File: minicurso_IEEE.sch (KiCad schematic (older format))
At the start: 5 parts

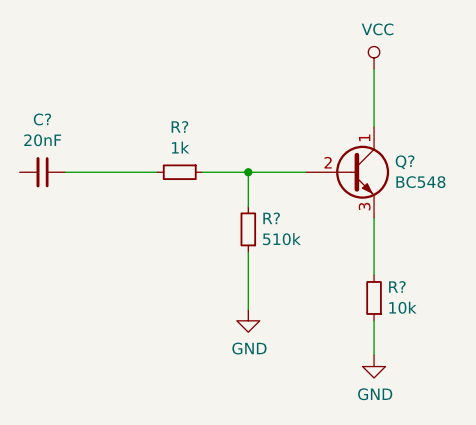
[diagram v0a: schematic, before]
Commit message: Parte-1 footprints
Foi adicionado os footprints dos componentes da primeira parte do projeto
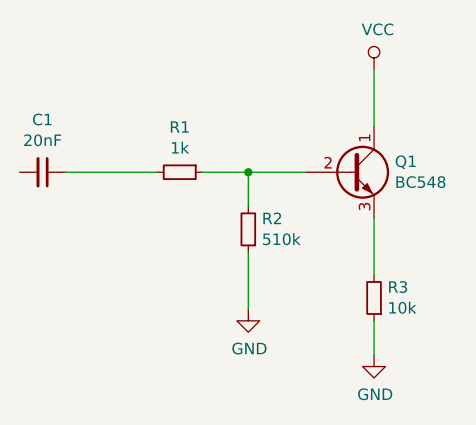
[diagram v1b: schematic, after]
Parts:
- C1: renamed from C?; footprint (none) -> Capacitor_THT:C_Disc_D3.0mm_W2.0mm_P2.50mm
- R1, R2, R3: renamed from R?; footprint (none) -> Resistor_THT:R_Axial_DIN0204_L3.6mm_D1.6mm_P7.62mm_Horizontal
- gave numbers to parts that had none: 1
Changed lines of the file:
@@
 $EndDescr
 $Comp
-L Device:R_Small R?
+L Device:R_Small R1
 U 1 1 5D4DF610
 P 1500 1700
-F 0 "R?" V 1304 1700 50  0000 C CNN
+F 0 "R1" V 1304 1700 50  0000 C CNN
 F 1 "1k" V 1395 1700 50  0000 C CNN
-F 2 "" H 1500 1700 50  0001 C CNN
+F 2 "Resistor_THT:R_Axial_DIN0204_L3.6mm_D1.6mm_P7.62mm_Horizontal" H 1500 1700 50  0001 C CNN
 F 3 "~" H 1500 1700 50  0001 C CNN
 	1    1500 1700
@@
 $EndComp
 $Comp
-L Device:C_Small C?
+L Device:C_Small C1
 U 1 1 5D4E0DE7
 P 900 1700
-F 0 "C?" V 671 1700 50  0000 C CNN
+F 0 "C1" V 671 1700 50  0000 C CNN
 F 1 "20nF" V 762 1700 50  0000 C CNN
-F 2 "" H 900 1700 50  0001 C CNN
+F 2 "Capacitor_THT:C_Disc_D3.0mm_W2.0mm_P2.50mm" H 900 1700 50  0001 C CNN
 F 3 "~" H 900 1700 50  0001 C CNN
 	1    900  1700
@@
 $EndComp
 $Comp
-L Device:R_Small R?
+L Device:R_Small R2
 U 1 1 5D4E1584
 P 1800 1950
-F 0 "R?" H 1741 1904 50  0000 R CNN
+F 0 "R2" H 1741 1904 50  0000 R CNN
 F 1 "510k" H 1741 1995 50  0000 R CNN
-F 2 "" H 1800 1950 50  0001 C CNN
+F 2 "Resistor_THT:R_Axial_DIN0204_L3.6mm_D1.6mm_P7.62mm_Horizontal" H 1800 1950 50  0001 C CNN
 F 3 "~" H 1800 1950 50  0001 C CNN
 	1    1800 1950
@@
 $EndComp
 $Comp
-L Transistor_BJT:BC548 Q?
+L Transistor_BJT:BC548 Q1
 U 1 1 5D4E1B29
 P 2250 1700
-F 0 "Q?" H 2441 1746 50  0000 L CNN
+F 0 "Q1" H 2441 1746 50  0000 L CNN
 F 1 "BC548" H 2441 1655 50  0000 L CNN
 F 2 "Package_TO_SOT_THT:TO-92_Inline" H 2450 1625 50  0001 L CIN
@@
 $EndComp
 $Comp
-L Device:R_Small R?
+L Device:R_Small R3
 U 1 1 5D4E20CF
 P 2350 2250
-F 0 "R?" H 2291 2204 50  0000 R CNN
+F 0 "R3" H 2291 2204 50  0000 R CNN
 F 1 "10k" H 2291 2295 50  0000 R CNN
-F 2 "" H 2350 2250 50  0001 C CNN
+F 2 "Resistor_THT:R_Axial_DIN0204_L3.6mm_D1.6mm_P7.62mm_Horizontal" H 2350 2250 50  0001 C CNN
 F 3 "~" H 2350 2250 50  0001 C CNN
 	1    2350 2250
@@
 $EndComp
 $Comp
-L power:GND #PWR?
+L power:GND #PWR0101
 U 1 1 5D4E3052
 P 2350 2500
-F 0 "#PWR?" H 2350 2250 50  0001 C CNN
+F 0 "#PWR0101" H 2350 2250 50  0001 C CNN
 F 1 "GND" H 2355 2327 50  0000 C CNN
 F 2 "" H 2350 2500 50  0001 C CNN
@@
 $EndComp
 $Comp
-L power:VCC #PWR?
+L power:VCC #PWR0102
 U 1 1 5D4E36BE
 P 2350 1250
-F 0 "#PWR?" H 2350 1100 50  0001 C CNN
+F 0 "#PWR0102" H 2350 1100 50  0001 C CNN
 F 1 "VCC" H 2367 1423 50  0000 C CNN
 F 2 "" H 2350 1250 50  0001 C CNN
@@
 	2350 2350 2350 2500
 $Comp
-L power:GND #PWR?
+L power:GND #PWR0103
 U 1 1 5D4E4E0D
 P 1800 2300
-F 0 "#PWR?" H 1800 2050 50  0001 C CNN
+F 0 "#PWR0103" H 1800 2050 50  0001 C CNN
 F 1 "GND" H 1805 2127 50  0000 C CNN
 F 2 "" H 1800 2300 50  0001 C CNN
